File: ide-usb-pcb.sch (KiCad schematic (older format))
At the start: 31 parts, among them J1 Conn_02x20_Odd_Even, J2 STM32F4_Discovery_Header, J3 Screw_Terminal_01x02, J4 USB_B, U1 TXS0108EPW, U2 TXS0108EPW

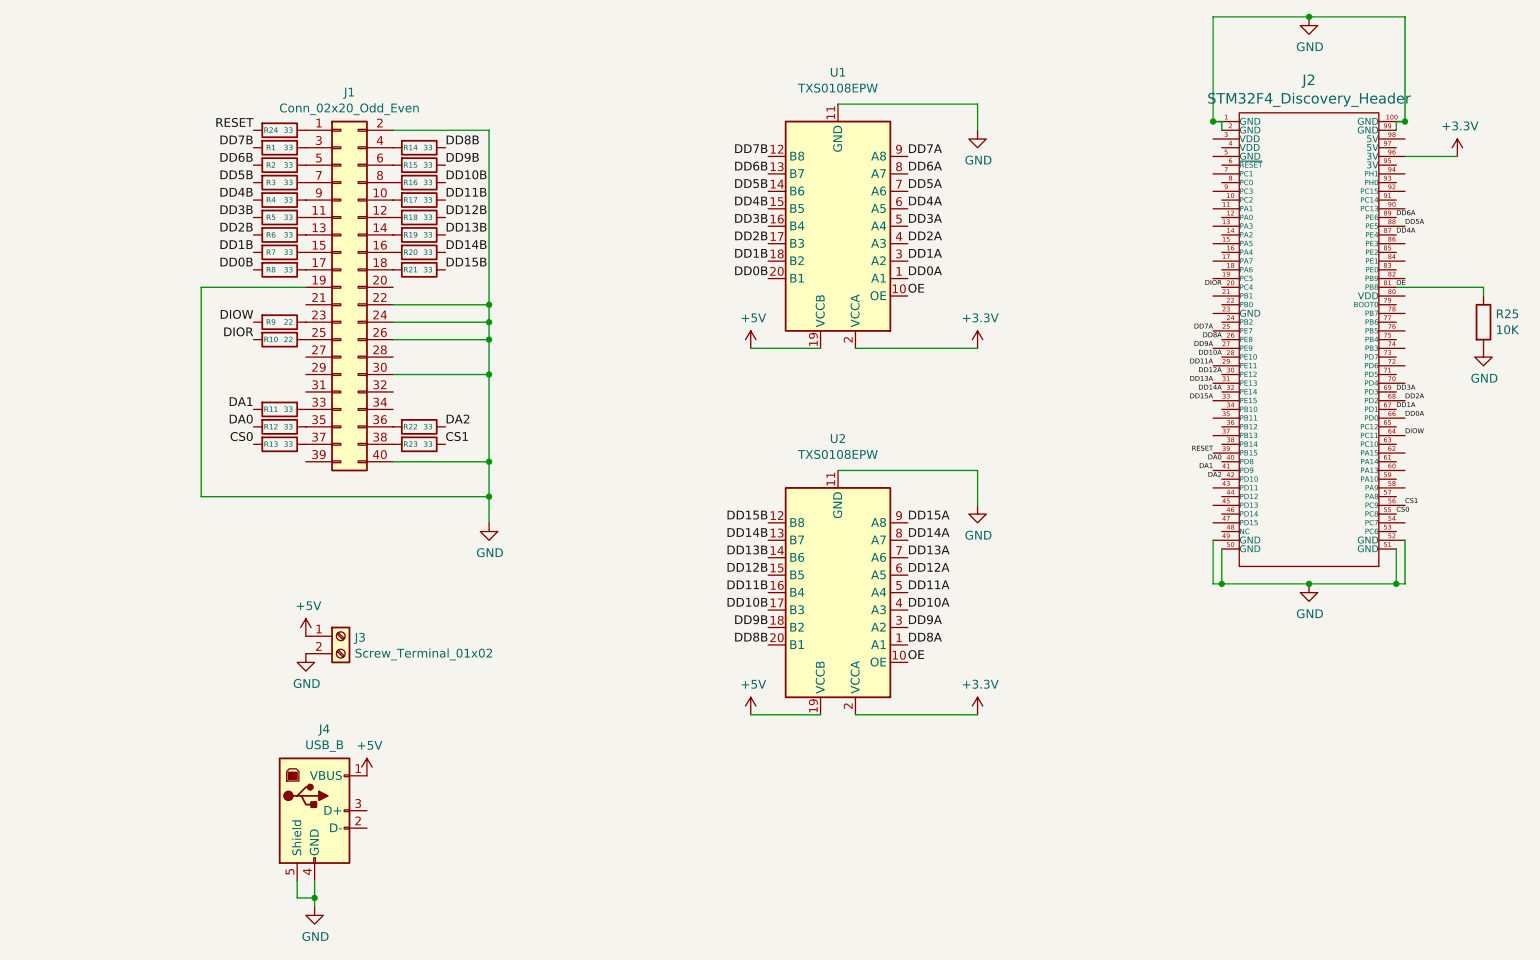
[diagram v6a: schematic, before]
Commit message: Improve spacing between some traces
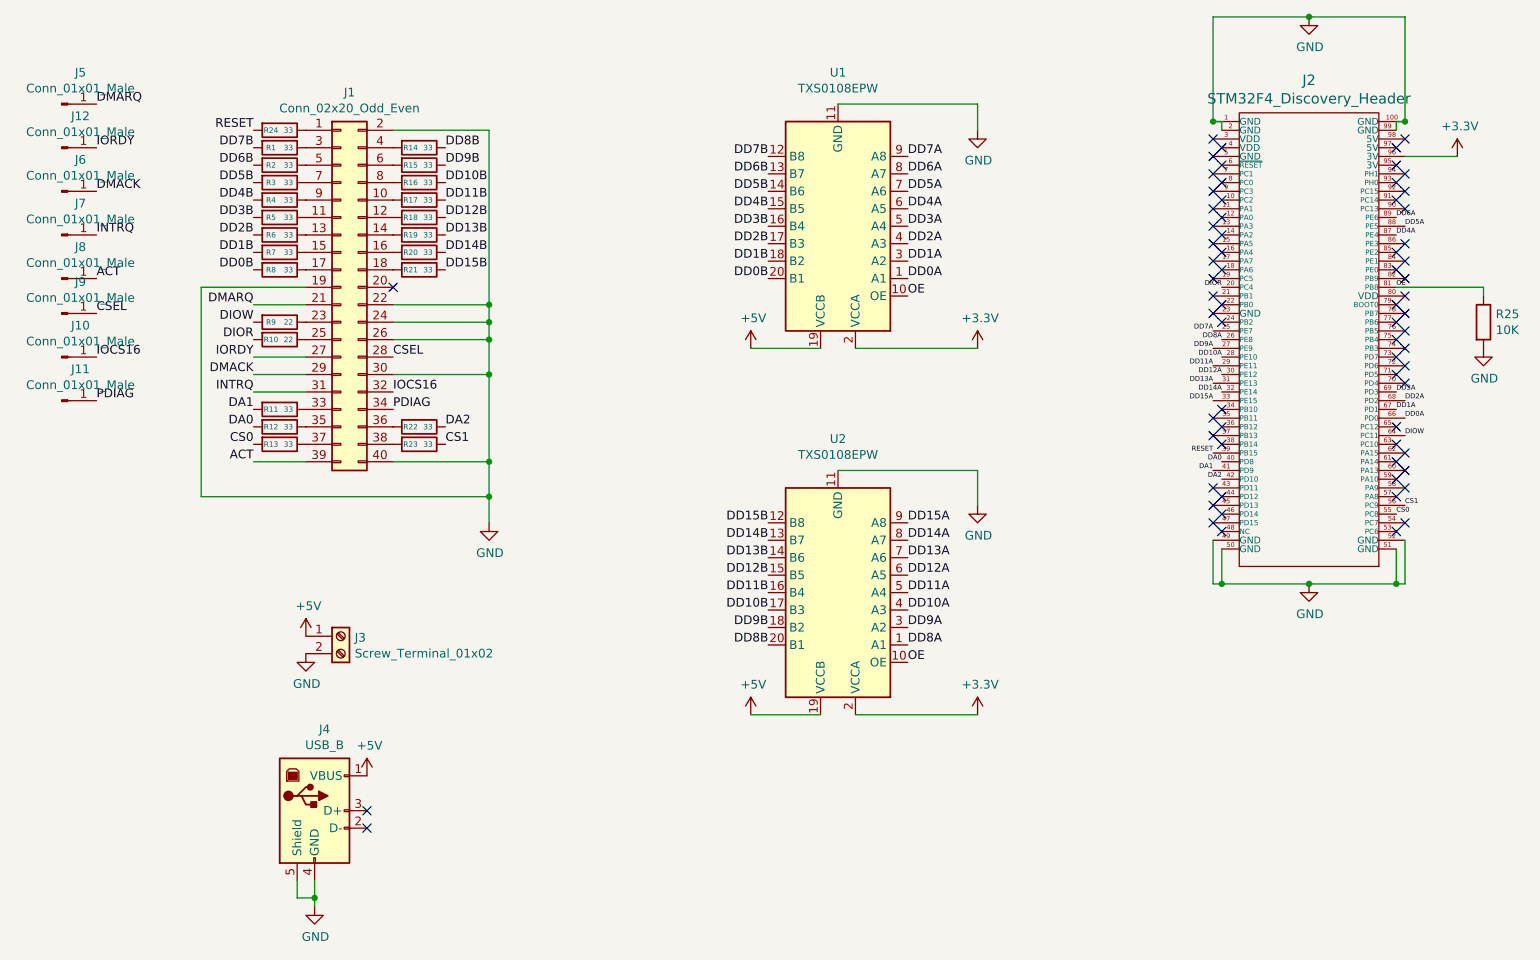
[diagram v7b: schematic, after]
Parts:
- added J10, J11, J12, J5, J6, J7, J8, J9: Conn_01x01_Male, Socket_Strips:Socket_Strip_Straight_1x01_Pitch2.54mm, symbol Connector:Conn_01x01_Male
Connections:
- net DMARQ: now reaches J1.21 (Pin_21)
- net DMARQ: now also J5.1 (Pin_1)
- net IORDY: now reaches J1.27 (Pin_27)
- net IORDY: now also J12.1 (Pin_1)
- net CSEL: now reaches J1.28 (Pin_28)
- net CSEL: now also J9.1 (Pin_1)
- net DMACK: now reaches J1.29 (Pin_29)
- net DMACK: now also J6.1 (Pin_1)
- net INTRQ: now reaches J1.31 (Pin_31)
- net INTRQ: now also J7.1 (Pin_1)
- net IOCS16: now reaches J1.32 (Pin_32)
- net IOCS16: now also J10.1 (Pin_1)
- net PDIAG: now reaches J1.34 (Pin_34)
- net PDIAG: now also J11.1 (Pin_1)
- net ACT: now reaches J1.39 (Pin_39)
- net ACT: now also J8.1 (Pin_1)
- no-connect marks 0 -> 69

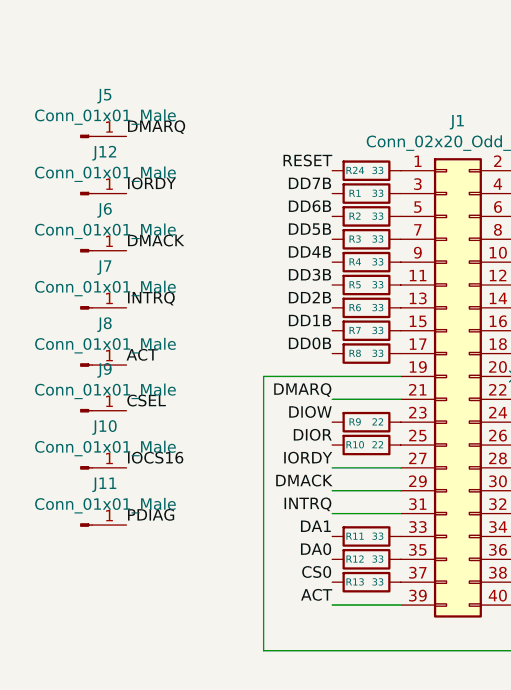
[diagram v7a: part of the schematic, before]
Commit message: Add connectors for unused IDE signals
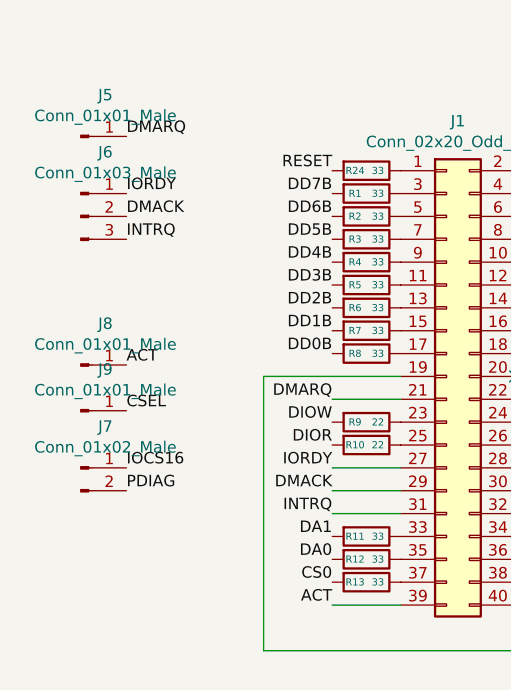
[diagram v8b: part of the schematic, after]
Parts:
- removed J10, J11, J12, J6, J7: Conn_01x01_Male, Socket_Strips:Socket_Strip_Straight_1x01_Pitch2.54mm, symbol Connector:Conn_01x01_Male
- added J6: Conn_01x03_Male, Socket_Strips:Socket_Strip_Straight_1x03_Pitch2.54mm, symbol Connector:Conn_01x03_Male
- added J7: Conn_01x02_Male, Socket_Strips:Socket_Strip_Straight_1x02_Pitch2.54mm, symbol Connector:Conn_01x02_Male
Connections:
- net DMACK: now also J6.2 (Pin_2)
- net INTRQ: now also J6.3 (Pin_3)
- net IOCS16: now also J7.1 (Pin_1)
- net IORDY: now also J6.1 (Pin_1)
- net PDIAG: now also J7.2 (Pin_2)
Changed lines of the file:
@@
 Text Label 1250 1350 0    50   ~ 0
 DMARQ
-$Comp
-L Connector:Conn_01x01_Male J6
-U 1 1 60EEE5DF
-P 1050 1850
-F 0 "J6" H 1158 2031 50  0000 C CNN
-F 1 "Conn_01x01_Male" H 1158 1940 50  0000 C CNN
-F 2 "Socket_Strips:Socket_Strip_Straight_1x01_Pitch2.54mm" H 1050 1850 50  0001 C CNN
-F 3 "~" H 1050 1850 50  0001 C CNN
-	1    1050 1850
-	1    0    0    -1
-$EndComp
-Text Label 1250 1850 0    50   ~ 0
+Text Label 1250 1700 0    50   ~ 0
 DMACK
-$Comp
-L Connector:Conn_01x01_Male J7
-U 1 1 60F0768E
-P 1050 2100
-F 0 "J7" H 1158 2281 50  0000 C CNN
-F 1 "Conn_01x01_Male" H 1158 2190 50  0000 C CNN
-F 2 "Socket_Strips:Socket_Strip_Straight_1x01_Pitch2.54mm" H 1050 2100 50  0001 C CNN
-F 3 "~" H 1050 2100 50  0001 C CNN
-	1    1050 2100
-	1    0    0    -1
-$EndComp
-Text Label 1250 2100 0    50   ~ 0
+Text Label 1250 1800 0    50   ~ 0
 INTRQ
 $Comp
@@
 Text Label 1250 2550 0    50   ~ 0
 CSEL
-$Comp
-L Connector:Conn_01x01_Male J10
-U 1 1 60F15E7A
-P 1050 2800
-F 0 "J10" H 1158 2981 50  0000 C CNN
-F 1 "Conn_01x01_Male" H 1158 2890 50  0000 C CNN
-F 2 "Socket_Strips:Socket_Strip_Straight_1x01_Pitch2.54mm" H 1050 2800 50  0001 C CNN
-F 3 "~" H 1050 2800 50  0001 C CNN
-	1    1050 2800
-	1    0    0    -1
-$EndComp
 Text Label 1250 2800 0    50   ~ 0
 IOCS16
-$Comp
-L Connector:Conn_01x01_Male J11
-U 1 1 60F15E81
-P 1050 3050
-F 0 "J11" H 1158 3231 50  0000 C CNN
-F 1 "Conn_01x01_Male" H 1158 3140 50  0000 C CNN
-F 2 "Socket_Strips:Socket_Strip_Straight_1x01_Pitch2.54mm" H 1050 3050 50  0001 C CNN
-F 3 "~" H 1050 3050 50  0001 C CNN
-	1    1050 3050
-	1    0    0    -1
-$EndComp
-Text Label 1250 3050 0    50   ~ 0
+Text Label 1250 2900 0    50   ~ 0
 PDIAG
 NoConn ~ 2950 2400
@@
 NoConn ~ 8700 1700
 NoConn ~ 7700 2000
-$Comp
-L Connector:Conn_01x01_Male J12
-U 1 1 60F839A6
-P 1050 1600
-F 0 "J12" H 1158 1781 50  0000 C CNN
-F 1 "Conn_01x01_Male" H 1158 1690 50  0000 C CNN
-F 2 "Socket_Strips:Socket_Strip_Straight_1x01_Pitch2.54mm" H 1050 1600 50  0001 C CNN
-F 3 "~" H 1050 1600 50  0001 C CNN
-	1    1050 1600
-	1    0    0    -1
-$EndComp
 Text Label 1250 1600 0    50   ~ 0
 IORDY
@@
 Wire Wire Line
 	5600 4850 6300 4850
+$Comp
+L Connector:Conn_01x03_Male J6
+U 1 1 60EBBB9D
+P 1050 1700
+F 0 "J6" H 1158 1981 50  0000 C CNN
+F 1 "Conn_01x03_Male" H 1158 1890 50  0000 C CNN
+F 2 "Socket_Strips:Socket_Strip_Straight_1x03_Pitch2.54mm" H 1050 1700 50  0001 C CNN
+F 3 "~" H 1050 1700 50  0001 C CNN
+	1    1050 1700
+	1    0    0    -1
+$EndComp
+$Comp
+L Connector:Conn_01x02_Male J7
+U 1 1 60EC64D1
+P 1050 2800
+F 0 "J7" H 1158 2981 50  0000 C CNN
+F 1 "Conn_01x02_Male" H 1158 2890 50  0000 C CNN
+F 2 "Socket_Strips:Socket_Strip_Straight_1x02_Pitch2.54mm" H 1050 2800 50  0001 C CNN
+F 3 "~" H 1050 2800 50  0001 C CNN
+	1    1050 2800
+	1    0    0    -1
+$EndComp
 $EndSCHEMATC
